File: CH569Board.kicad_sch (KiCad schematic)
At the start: 38 parts, among them CN1 BA42-80BT-1-NHB, J1 Conn_01x02_Male, J2 Conn_01x03_Male, U1 AMS1117-3.3, U3 AMS1117-1.2, U4 W25Q32JVSSIQ, X1 O705030MEEA4SC

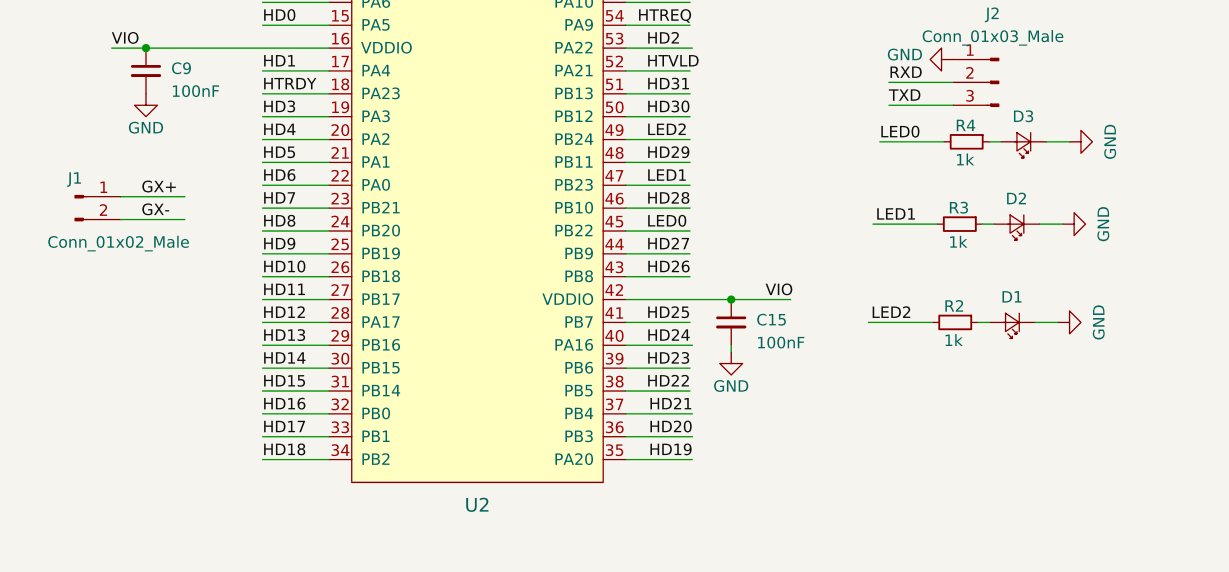
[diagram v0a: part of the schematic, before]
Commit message: New Edge cuts from FreeCAD and match the board to FPGA main board
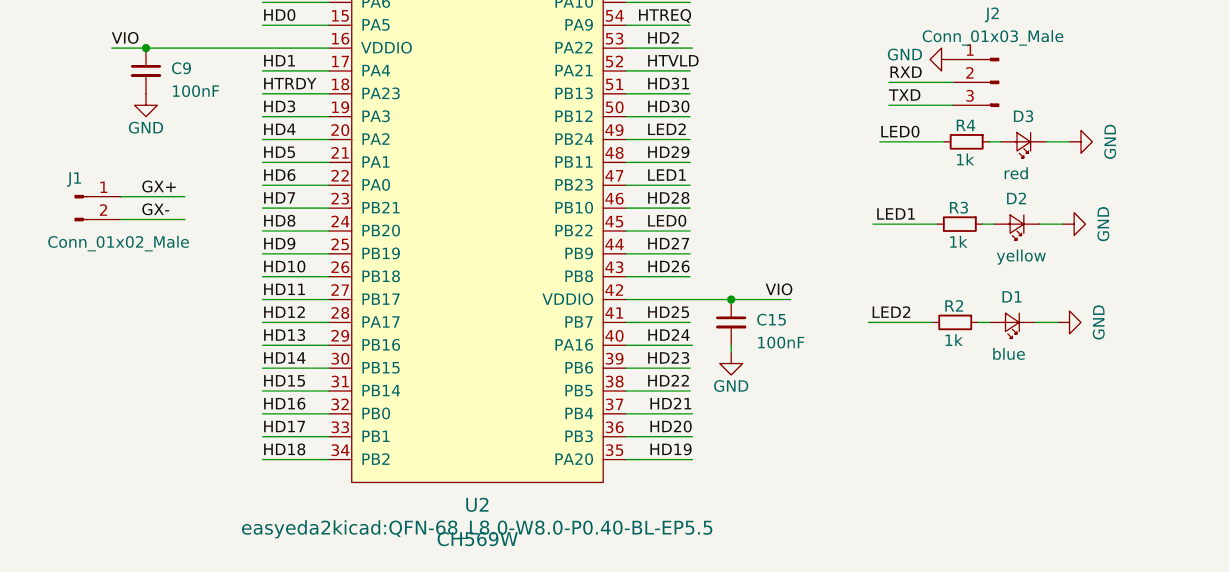
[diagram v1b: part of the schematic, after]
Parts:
- D1: value (none) -> blue; footprint (none) -> LED_SMD:LED_0603_1608Metric
- D2: value (none) -> yellow; footprint (none) -> LED_SMD:LED_0603_1608Metric
- D3: value (none) -> red; footprint (none) -> LED_SMD:LED_0603_1608Metric
- U2: value (none) -> CH569W; footprint (none) -> easyeda2kicad:QFN-68_L8.0-W8.0-P0.40-BL-EP5.5
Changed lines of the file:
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@@
       (effects (font (size 1.27 1.27)) (justify right))
     )
-    (property "Value" "" (id 1) (at 191.262 152.4 0)
+    (property "Value" "yellow" (id 1) (at 191.262 152.4 0)
       (effects (font (size 1.27 1.27)) (justify right))
     )
-    (property "Footprint" "" (id 2) (at 193.548 148.844 90)
+    (property "Footprint" "LED_SMD:LED_0603_1608Metric" (id 2) (at 193.548 148.844 90)
       (effects (font (size 1.27 1.27)) hide)
     )
@@
       (effects (font (size 1.27 1.27)) (justify right))
     )
-    (property "Value" "" (id 1) (at 190.754 163.322 0)
+    (property "Value" "blue" (id 1) (at 190.754 163.322 0)
       (effects (font (size 1.27 1.27)) (justify right))
     )
-    (property "Footprint" "" (id 2) (at 193.04 159.766 90)
+    (property "Footprint" "LED_SMD:LED_0603_1608Metric" (id 2) (at 193.04 159.766 90)
       (effects (font (size 1.27 1.27)) hide)
     )
@@
       (effects (font (size 1.524 1.524)))
     )
-    (property "Value" "" (id 1) (at 133.604 183.896 0)
+    (property "Value" "CH569W" (id 1) (at 133.604 183.896 0)
       (effects (font (size 1.524 1.524)))
     )
-    (property "Footprint" "" (id 2) (at 133.604 182.626 0)
+    (property "Footprint" "easyeda2kicad:QFN-68_L8.0-W8.0-P0.40-BL-EP5.5" (id 2) (at 133.604 182.626 0)
       (effects (font (size 1.524 1.524)))
     )
@@
       (effects (font (size 1.27 1.27)) (justify right))
     )
-    (property "Value" "" (id 1) (at 192.024 143.256 0)
+    (property "Value" "red" (id 1) (at 192.024 143.256 0)
       (effects (font (size 1.27 1.27)) (justify right))
     )
-    (property "Footprint" "" (id 2) (at 194.31 139.7 90)
-      (effects (font (size 1.27 1.27)) hide)
-    )
+    (property "Footprint" "LED_SMD:LED_0603_1608Metric" (id 2) (at 194.31 139.7 90)
+      (effects (font (size 1.27 1.27)) hide)
+    )

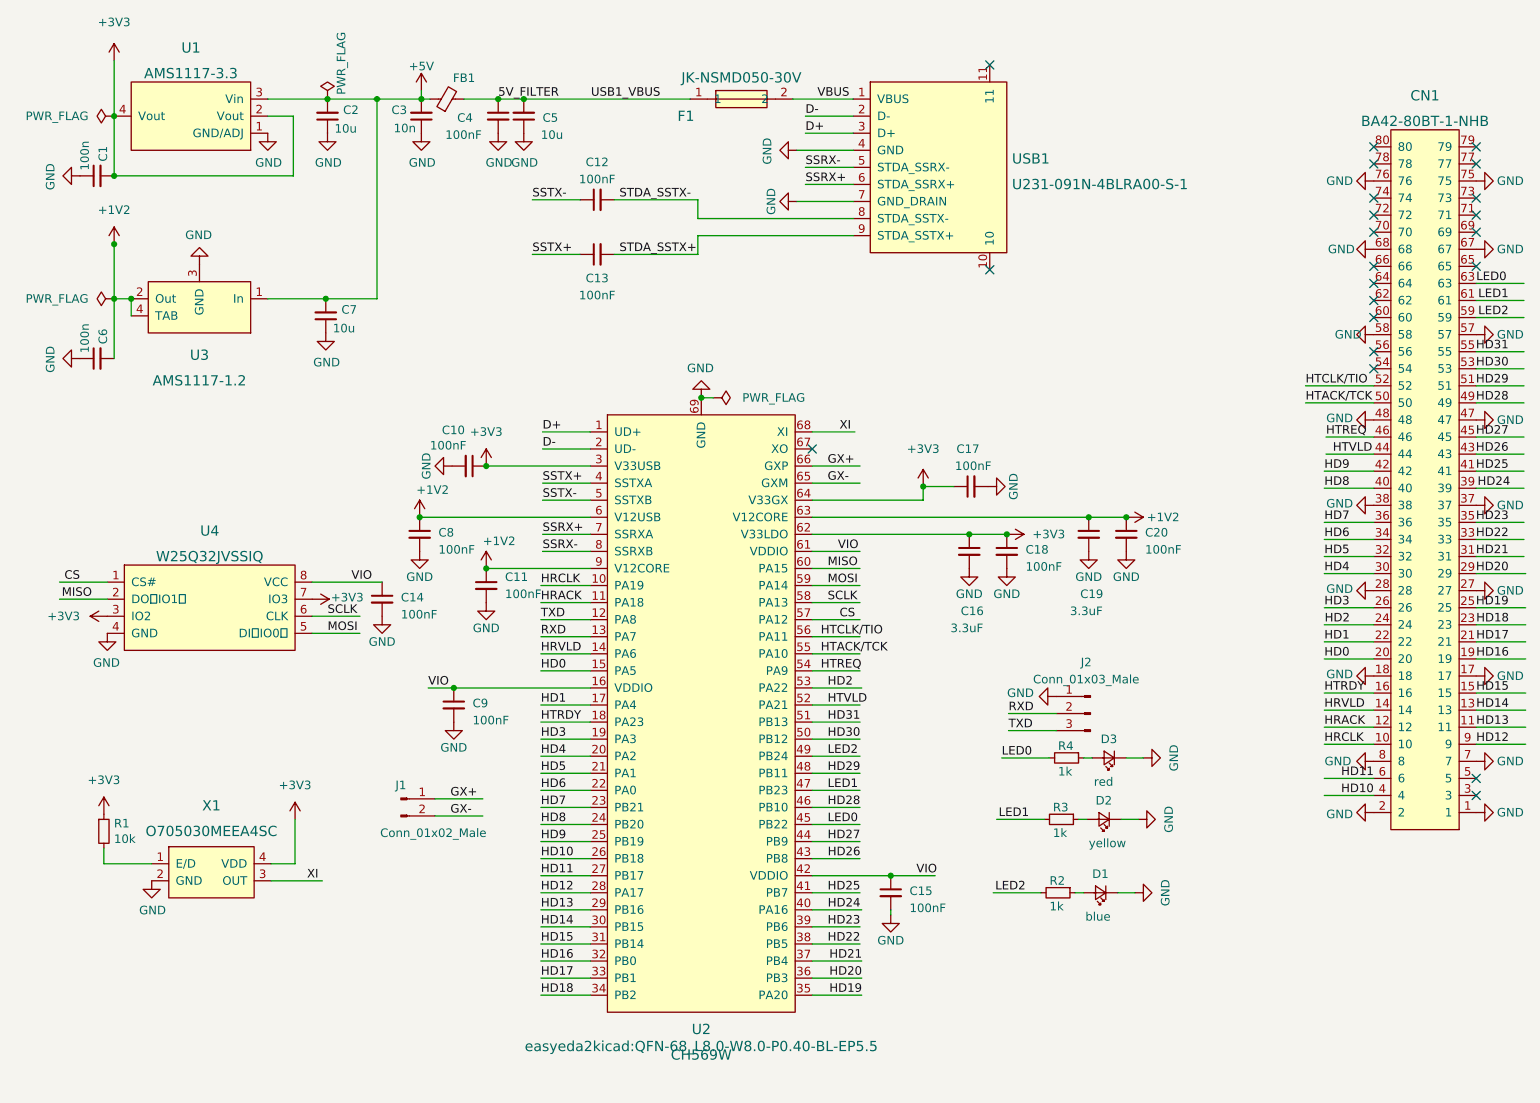
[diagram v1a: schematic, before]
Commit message: Big design fixup: Make Layer 3 a GND plane so signals reference ground. Eliminate one LED for better integrity of the signal traces, new board outline
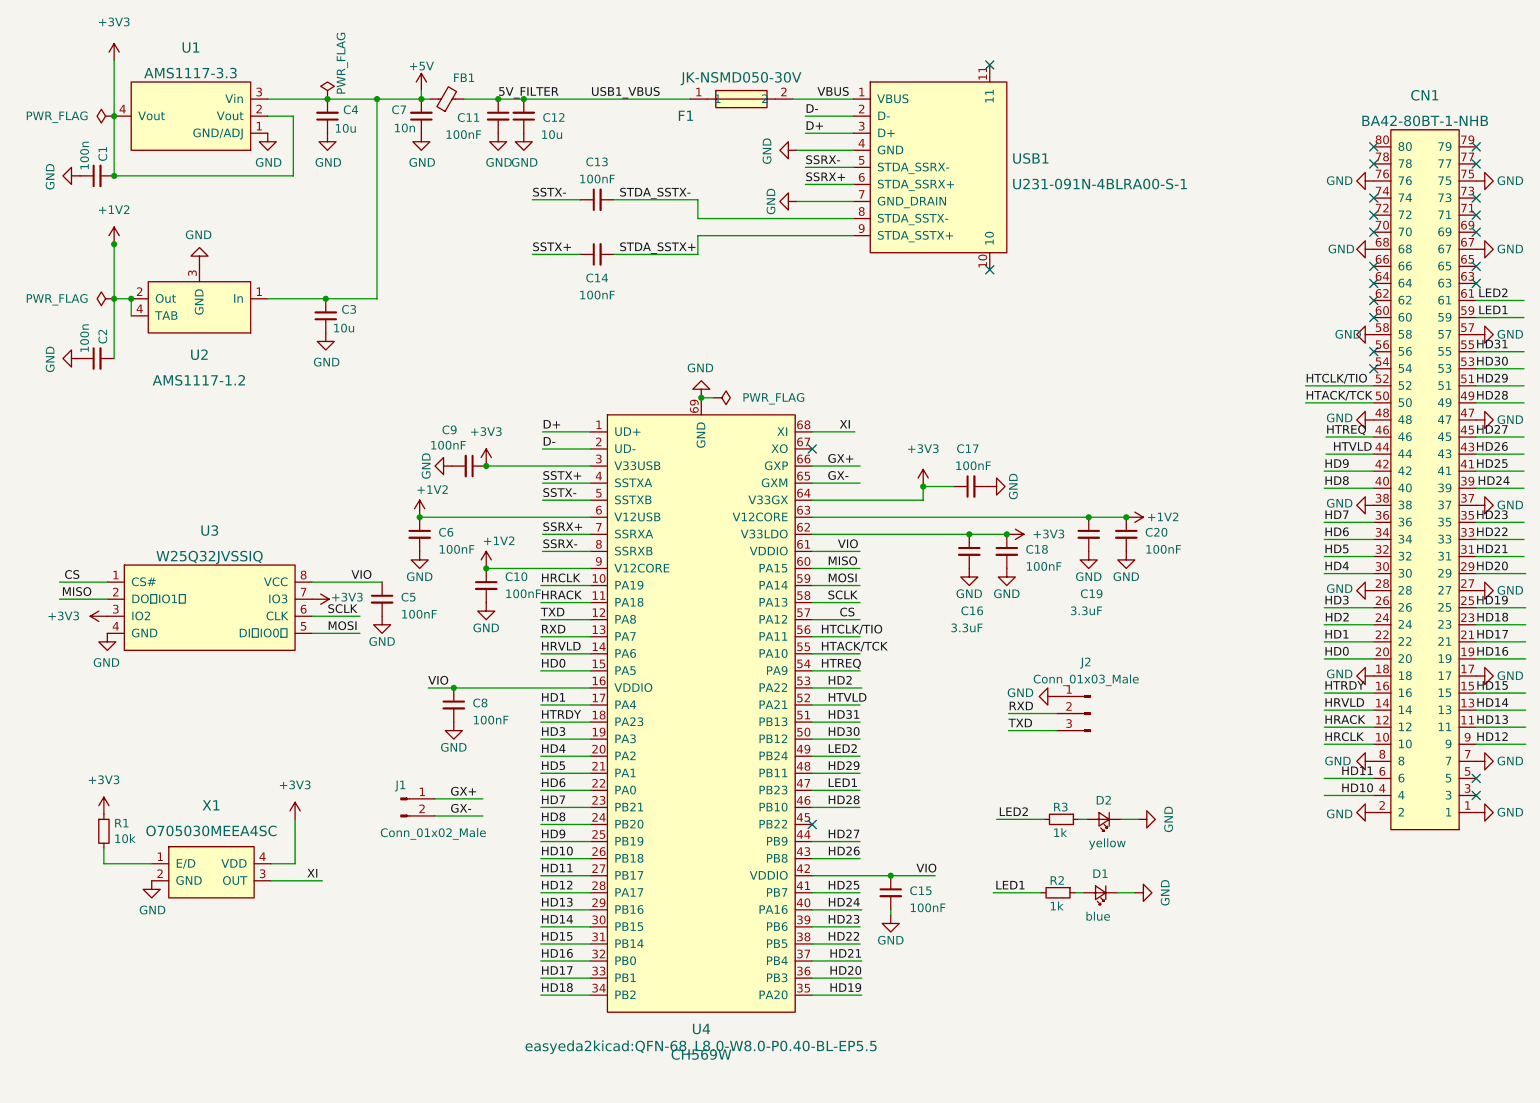
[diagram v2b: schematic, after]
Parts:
- removed D3: red, LED_SMD:LED_0603_1608Metric, symbol Device:LED_Small
- removed R4: 1k, Resistor_SMD:R_0603_1608Metric, symbol Device:R_Small
- renumbered C11 to C10, C4 to C11, C5 to C12, C12 to C13, C13 to C14, C6 to C2, C7 to C3, C2 to C4, C14 to C5, C8 to C6, C3 to C7, C9 to C8, C10 to C9, U3 to U2, U4 to U3, U2 to U4
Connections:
- net LED1: now also CN1.59, R2.2; no longer CN1.61, R3.2
- net LED2: now also CN1.61, R3.2; no longer CN1.59, R2.2
- net LED0: no longer names the net of CN1.63
- net LED0: no longer U4.45 (PB22)
- no-connect marks 22 -> 24

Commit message: Fix swapped pins 1 and 3 on the 1.2V regulator
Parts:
- U2: value AMS1117-1.2 -> (none); footprint easyeda2kicad:SOT-223-4_L6.5-W3.5-P2.30-LS7.0-BR -> SOT-223-4_L6.5-W3.5-P2.30-LS7.0-BR
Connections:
- net +5V: now also U2.3 (In); no longer U2.1 (In)
- net GND: now also U2.1 (GND); no longer U2.3 (GND)
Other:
- moved on the sheet: C3
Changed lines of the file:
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@@
   (junction (at 101.6 96.266) (diameter 0) (color 0 0 0 0)
   )
-  (junction (at 77.724 71.374) (diameter 0) (color 0 0 0 0)
-  )
   (junction (at 46.228 71.374) (diameter 0) (color 0 0 0 0)
   )
@@
   (junction (at 196.85 103.886) (diameter 0) (color 0 0 0 0)
   )
+  (junction (at 85.344 66.294) (diameter 0) (color 0 0 0 0)
+  )
   (junction (at 96.774 129.286) (diameter 0) (color 0 0 0 0)
   )
@@
   (junction (at 46.228 44.196) (diameter 0) (color 0 0 0 0)
   )
+  (junction (at 58.928 66.294) (diameter 0) (color 0 0 0 0)
+  )
   (junction (at 173.482 106.426) (diameter 0) (color 0 0 0 0)
   )
@@
     (stroke (width 0) (type default) (color 0 0 0 0))
   )
-  (wire (pts (xy 69.088 71.374) (xy 77.724 71.374))
-    (stroke (width 0) (type default) (color 0 0 0 0))
-  )
   (wire (pts (xy 157.226 111.506) (xy 150.114 111.506))
     (stroke (width 0) (type default) (color 0 0 0 0))
@@
     (stroke (width 0) (type default) (color 0 0 0 0))
   )
+  (wire (pts (xy 58.674 66.294) (xy 58.928 66.294))
+    (stroke (width 0) (type default) (color 0 0 0 0))
+  )
   (wire (pts (xy 157.226 121.666) (xy 150.114 121.666))
     (stroke (width 0) (type default) (color 0 0 0 0))
@@
     (stroke (width 0) (type default) (color 0 0 0 0))
   )
-  (wire (pts (xy 85.344 71.374) (xy 85.344 41.656))
+  (wire (pts (xy 85.344 71.374) (xy 85.344 66.294))
     (stroke (width 0) (type default) (color 0 0 0 0))
   )
@@
     (stroke (width 0) (type default) (color 0 0 0 0))
   )
-  (wire (pts (xy 223.52 84.328) (xy 233.68 84.328))
+  (wire (pts (xy 85.344 66.294) (xy 85.344 41.656))
     (stroke (width 0) (type default) (color 0 0 0 0))
   )
-  (wire (pts (xy 77.724 71.374) (xy 85.344 71.374))
+  (wire (pts (xy 223.52 84.328) (xy 233.68 84.328))
     (stroke (width 0) (type default) (color 0 0 0 0))
   )
@@
     (stroke (width 0) (type default) (color 0 0 0 0))
   )
+  (wire (pts (xy 58.928 66.294) (xy 85.344 66.294))
+    (stroke (width 0) (type default) (color 0 0 0 0))
+  )
   (wire (pts (xy 107.188 41.656) (xy 131.953 41.656))
     (stroke (width 0) (type default) (color 0 0 0 0))
@@
     (pin "1")
   )
-  (symbol (lib_id "Device:C_Small") (at 77.724 73.914 180) (unit 1)
+  (symbol (lib_id "Device:C_Small") (at 85.344 73.914 180) (unit 1)
     (in_bom yes) (on_board yes)
-    (property "Reference" "C3" (id 0) (at 80.0482 73.0055 0)
+    (property "Reference" "C3" (id 0) (at 87.6682 73.0055 0)
       (effects (font (size 1.27 1.27)) (justify right))
     )
-    (property "Value" "10u" (id 1) (at 78.7782 75.7806 0)
+    (property "Value" "10u" (id 1) (at 86.3982 75.7806 0)
       (effects (font (size 1.27 1.27)) (justify right))
     )
-    (property "Footprint" "Capacitor_SMD:C_0805_2012Metric" (id 2) (at 77.724 73.914 0)
+    (property "Footprint" "Capacitor_SMD:C_0805_2012Metric" (id 2) (at 85.344 73.914 0)
       (effects (font (size 1.27 1.27)) hide)
     )
-    (property "Datasheet" "~" (id 3) (at 77.724 73.914 0)
+    (property "Datasheet" "~" (id 3) (at 85.344 73.914 0)
       (effects (font (size 1.27 1.27)) hide)
     )
-    (property "LCSC" "C15850" (id 4) (at 77.724 73.914 0)
+    (property "LCSC" "C15850" (id 4) (at 85.344 73.914 0)
       (effects (font (size 1.27 1.27)) hide)
     )
@@
     (pin "1")
   )
-  (symbol (lib_id "power:GND") (at 77.724 76.454 0) (unit 1)
+  (symbol (lib_id "power:GND") (at 85.344 76.454 0) (unit 1)
     (in_bom yes) (on_board yes)
-    (property "Reference" "#PWR013" (id 0) (at 77.724 82.804 0)
+    (property "Reference" "#PWR013" (id 0) (at 85.344 82.804 0)
       (effects (font (size 1.27 1.27)) hide)
     )
-    (property "Value" "GND" (id 1) (at 77.851 80.8482 0))
-    (property "Footprint" "" (id 2) (at 77.724 76.454 0)
+    (property "Value" "GND" (id 1) (at 85.471 80.8482 0))
+    (property "Footprint" "" (id 2) (at 85.344 76.454 0)
       (effects (font (size 1.27 1.27)) hide)
     )
-    (property "Datasheet" "" (id 3) (at 77.724 76.454 0)
+    (property "Datasheet" "" (id 3) (at 85.344 76.454 0)
       (effects (font (size 1.27 1.27)) hide)
     )
@@
     (pin "1")
   )
-  (symbol (lib_id "power:GND") (at 58.928 66.294 180) (unit 1)
+  (symbol (lib_id "power:GND") (at 69.088 71.374 0) (unit 1)
     (in_bom yes) (on_board yes)
-    (property "Reference" "#PWR09" (id 0) (at 58.928 59.944 0)
+    (property "Reference" "#PWR09" (id 0) (at 69.088 77.724 0)
       (effects (font (size 1.27 1.27)) hide)
     )
-    (property "Value" "GND" (id 1) (at 58.801 61.8998 0))
-    (property "Footprint" "" (id 2) (at 58.928 66.294 0)
+    (property "Value" "GND" (id 1) (at 69.215 75.7682 0))
+    (property "Footprint" "" (id 2) (at 69.088 71.374 0)
       (effects (font (size 1.27 1.27)) hide)
     )
-    (property "Datasheet" "" (id 3) (at 58.928 66.294 0)
+    (property "Datasheet" "" (id 3) (at 69.088 71.374 0)
       (effects (font (size 1.27 1.27)) hide)
     )
@@
       (effects (font (size 1.524 1.524)))
     )
-    (property "Value" "AMS1117-1.2" (id 1) (at 58.928 83.566 0)
+    (property "Value" "" (id 1) (at 58.928 83.566 0)
       (effects (font (size 1.524 1.524)))
     )
-    (property "Footprint" "easyeda2kicad:SOT-223-4_L6.5-W3.5-P2.30-LS7.0-BR" (id 2) (at 58.928 58.674 0)
+    (property "Footprint" "SOT-223-4_L6.5-W3.5-P2.30-LS7.0-BR" (id 2) (at 58.928 58.674 0)
       (effects (font (size 1.524 1.524)) hide)
     )
@@
     )
     (path "/f1fe9332-8e34-48c2-b155-1eb943f22300"
-      (reference "U2") (unit 1) (value "AMS1117-1.2") (footprint "easyeda2kicad:SOT-223-4_L6.5-W3.5-P2.30-LS7.0-BR")
+      (reference "U2") (unit 1) (value "AMS1117-1.2") (footprint "SOT-223-4_L6.5-W3.5-P2.30-LS7.0-BR")
     )
     (path "/658da924-21b9-44a8-a0b5-52d675bc69e1"
